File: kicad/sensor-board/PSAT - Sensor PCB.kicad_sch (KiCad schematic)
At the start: 19 parts, among them J1 MCU - Conn_01x01, J2 Conn_01x02, J3 MCU - Conn_01x02, J4 MCU - Conn_01x04, J5 Conn_01x01, U1 MPU-6000, U2 BME280

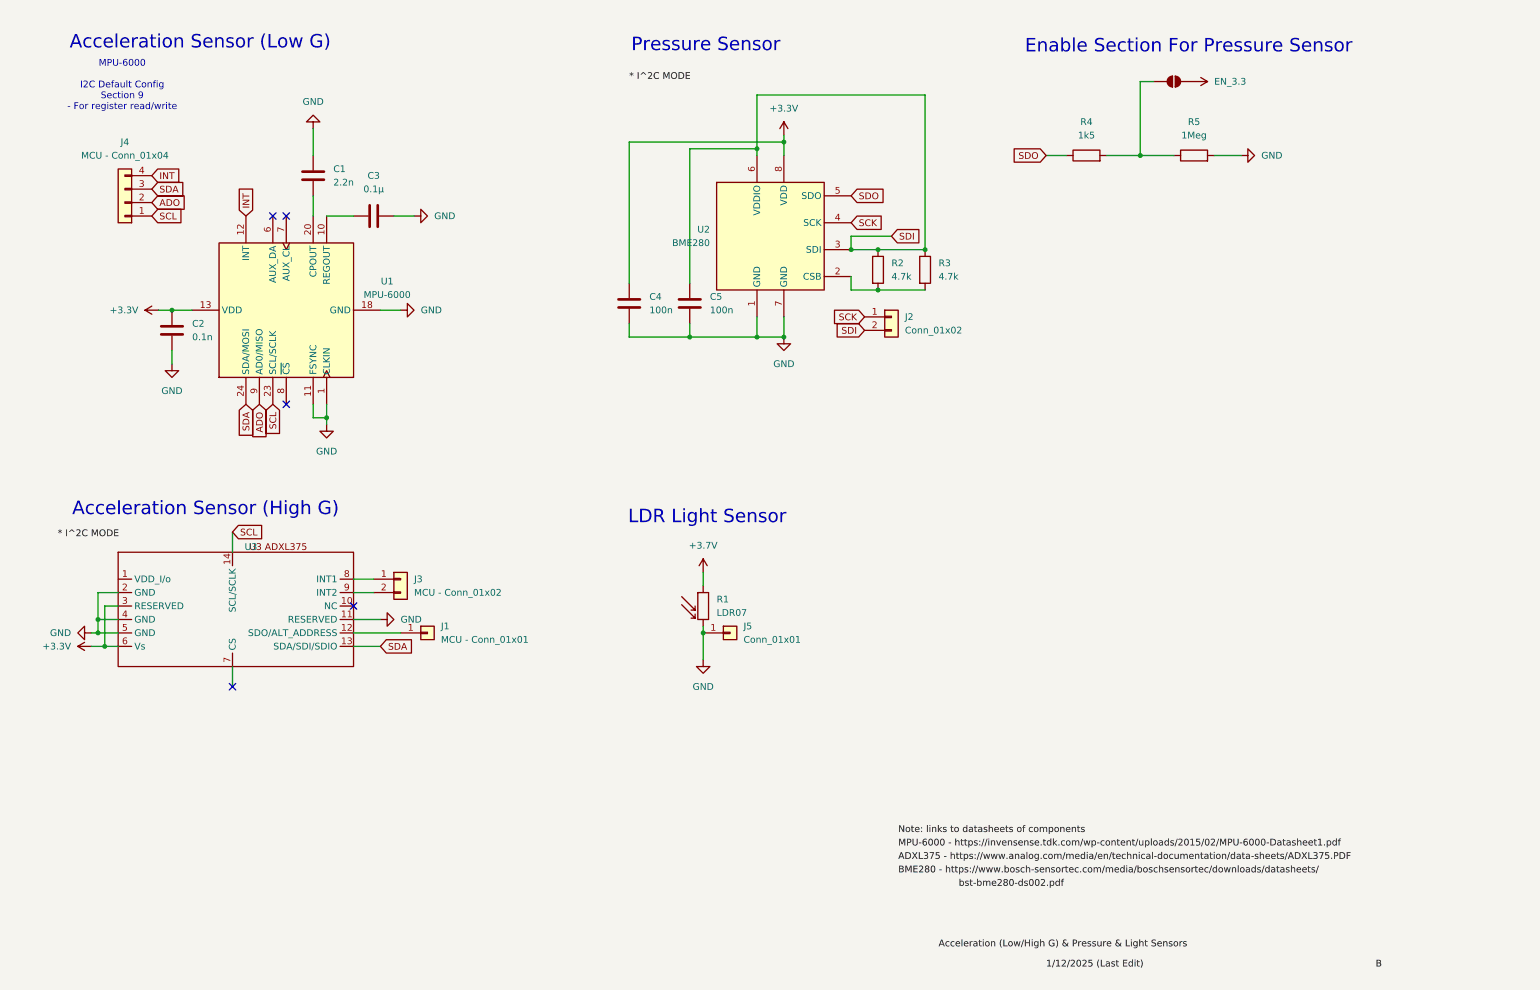
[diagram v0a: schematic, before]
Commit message: feat: sensor board schematic and started pcb
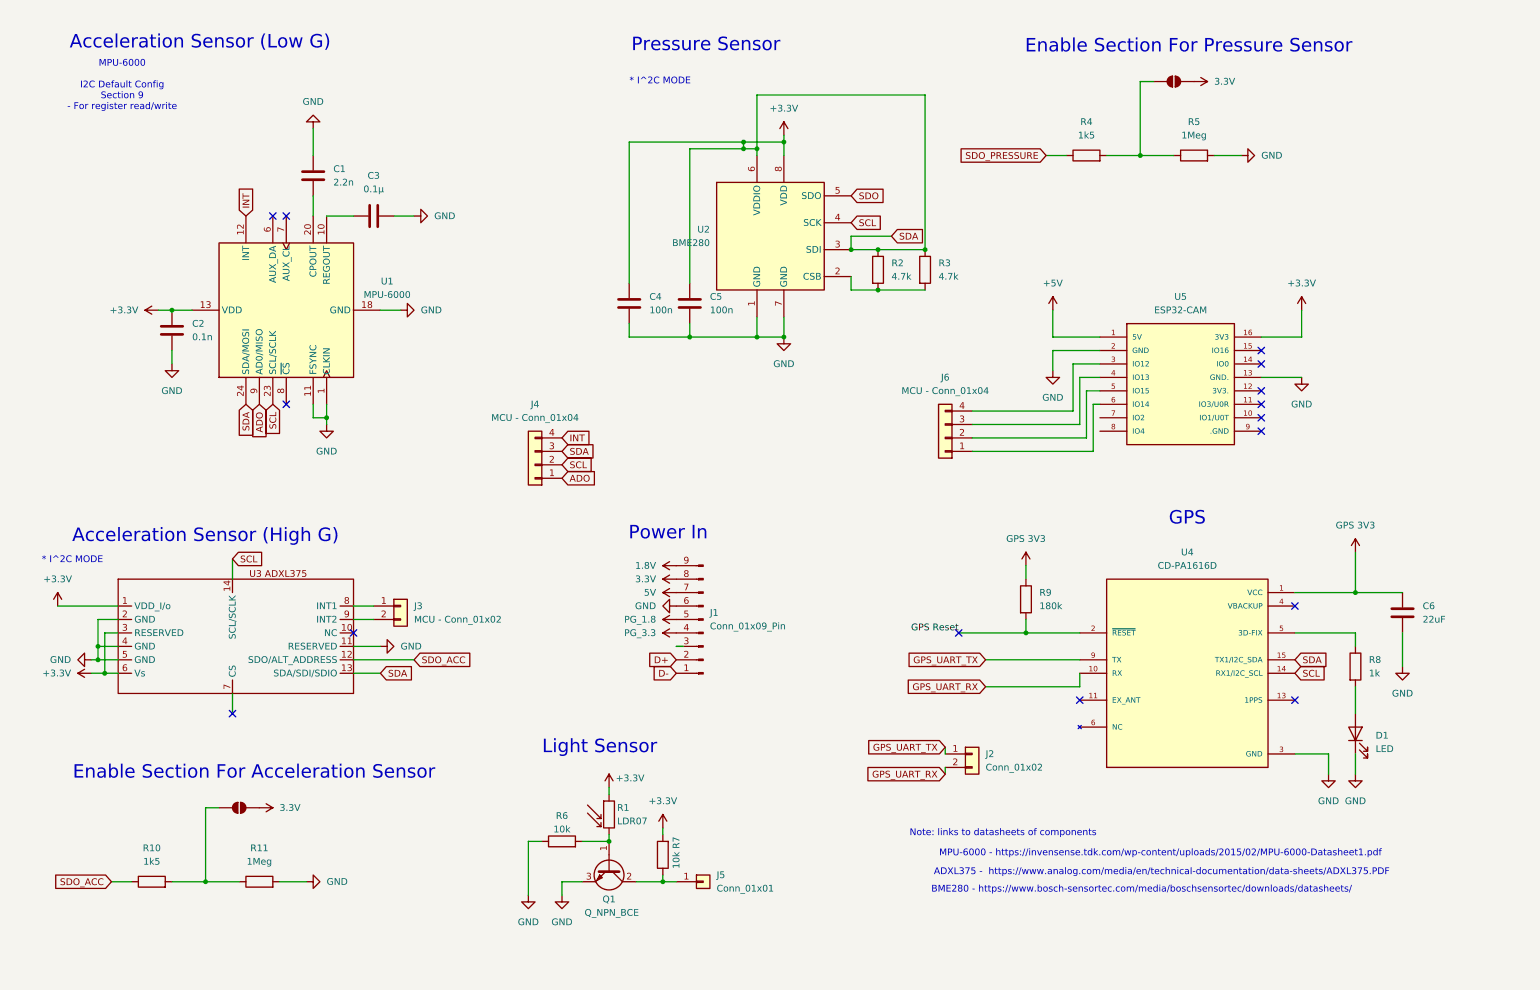
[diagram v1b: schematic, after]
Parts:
- removed J1: MCU - Conn_01x01, symbol Connector_Generic:Conn_01x01
- added C6: 22uF, Capacitor_SMD:C_0805_2012Metric_Pad1.18x1.45mm_HandSolder, symbol Device:C
- added D1: LED, LED_SMD:LED_LiteOn_LTST-C19HE1WT, symbol Device:LED
- added J1: Conn_01x09_Pin, Connector_PinHeader_2.54mm:PinHeader_1x09_P2.54mm_Vertical, symbol Connector:Conn_01x09_Pin
- added J6: MCU - Conn_01x04, Connector_PinHeader_2.54mm:PinHeader_1x04_P2.54mm_Vertical, symbol Connector_Generic:Conn_01x04
- added JP2: EN_5, Jumper:SolderJumper-2_P1.3mm_Open_Pad1.0x1.5mm, symbol Jumper:SolderJumper_2_Open
- added Q1: Q_NPN_BCE, Package_TO_SOT_SMD:SOT-23-3, symbol Transistor_BJT:Q_NPN_BCE
- added R10: 1k5, Resistor_SMD:R_0805_2012Metric_Pad1.20x1.40mm_HandSolder, symbol Device:R
- added R11: 1Meg, Resistor_SMD:R_0805_2012Metric_Pad1.20x1.40mm_HandSolder, symbol Device:R
- added R6, R7: 10k, Resistor_SMD:R_0805_2012Metric_Pad1.20x1.40mm_HandSolder, symbol Device:R
- added R8: 1k, Resistor_SMD:R_0805_2012Metric_Pad1.20x1.40mm_HandSolder, symbol Device:R
- added R9: 180k, Resistor_SMD:R_0805_2012Metric_Pad1.20x1.40mm_HandSolder, symbol Device:R
- added U4: CD-PA1616D, gps:XCVR_CD-PA1616D, symbol CD-PA1616D:CD-PA1616D
- added U5: ESP32-CAM, Connector_PinSocket_2.54mm:ESPCam, symbol ESP32-CAM:ESP32-CAM
- J2, J3: footprint (none) -> Connector_PinHeader_2.54mm:PinHeader_1x02_P2.54mm_Vertical
- J4: footprint (none) -> Connector_PinHeader_2.54mm:PinHeader_1x04_P2.54mm_Vertical
- J5: footprint (none) -> Connector_PinHeader_2.54mm:PinHeader_1x01_P2.54mm_Vertical
- R4, R5: footprint Resistor_SMD:R_0402_1005Metric -> Resistor_SMD:R_0805_2012Metric_Pad1.20x1.40mm_HandSolder
- U1: footprint (none) -> mpu6000:QFN-24-EP
- U2: footprint (none) -> bme280:PSON65P250X250X100-8N
- U3: value ~ -> ADXL375; footprint ADXL375:0805 CAP -> ADXL375:PQFN80P500X300X100-14N
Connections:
- net +3.7V is gone; now on net +3.3V: R1.1
- net SDA is gone; now on net +3.3V: J4.3 (Pin_3), U1.24 (SDA/MOSI), U3.13 (SDA/SDI/SDIO)
- net +3.3V: now also C5.1, R2.1, R3.1, U2.3 (SDI), U2.6 (VDDIO), U3.1 (VDD_I/o), R7.2, U4.15 (TX1/I2C_SDA), U5.16 (3V3)
- net ADO: now also J4.1 (Pin_1); no longer J4.2 (Pin_2)
- net GND: now also C6.2, D1.1 (K), J1.6 (Pin_6), Q1.3 (E), R11.2, R6.1, U4.12 (GND), U4.19 (GND), U4.3 (GND), U4.8 (GND), U5.13 (GND.), U5.2 (GND); no longer J5.1 (Pin_1), R1.2
- net SCL: now also J4.2 (Pin_2), U2.4 (SCK), U4.14 (RX1/I2C_SCL); no longer J4.1 (Pin_1)
- net SDO: no longer R4.1
- net SDO_ACC: now reaches U3.12 (SDO/ALT_ADDRESS)
- net SDO_ACC: now also R10.1
- net EN_3.3 renamed 3.3V
- net 3.3V: now also J1.8 (Pin_8), JP2.1 (A)
- net SCK renamed GPS_UART_TX
- net GPS_UART_TX: now also U4.9 (TX); no longer U2.4 (SCK)
- removed net SDI: C5.1, J2.2 (Pin_2), R2.1, R3.1, U2.3 (SDI), U2.6 (VDDIO)
- new net: D1.2 (A), R8.2
- new net: Q1.1 (B), R1.2, R6.2
- new net: J6.4 (Pin_4), U5.3 (IO12)
- new net: J6.3 (Pin_3), U5.4 (IO13)
- new net: J6.2 (Pin_2), U5.5 (IO15)
- new net: J6.1 (Pin_1), U5.6 (IO14)
- new net: U4.16 (NC), U4.17 (NC), U4.18 (NC), U4.20 (NC), U4.6 (NC), U4.7 (NC)
- new net: R8.1, U4.5 (3D-FIX)
- new net: J5.1 (Pin_1), Q1.2 (C), R7.1
- new net: JP2.2 (B), R10.2, R11.1
- new net +5V: U5.1 (5V)
- new net 1.8V: J1.9 (Pin_9)
- new net 5V: J1.7 (Pin_7)
- new net D+: J1.2 (Pin_2)
- new net D-: J1.1 (Pin_1)
- new net GPS 3V3: C6.1, R9.1, U4.1 (VCC)
- new net GPS Reset: R9.2, U4.2 (~{RESET})
- new net GPS_UART_RX: J2.2 (Pin_2), U4.10 (RX)
- new net PG_1.8: J1.5 (Pin_5)
- new net PG_3.3: J1.4 (Pin_4)
- new net SDO_PRESSURE: R4.1
- no-connect marks 5 -> 15
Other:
- note added: "* I^2C MODE"
- note added: "ADXL375 - https://www.analog.com/media/en/technical-documentation/data-sheets/ADXL375.PDF"
- note added: "BME280 - https://www.bosch-sensortec.com/media/boschsensortec/downloads/datasheets/"
- note added: "Enable Section For Acceleration Sensor"
- note added: "GPS"
- note added: "Light Sensor"
- note added: "MPU-6000 - https://invensense.tdk.com/wp-content/uploads/2015/02/MPU-6000-Datasheet1.pdf"
- note added: "Note: links to datasheets of components"
- note added: "Power In"
- note removed: "LDR Light Sensor"
- title: (none) -> Acceleration (Low/High G), Pressure, Light and GPS Sensors
- moved on the sheet: J2, J3, J4, J5, R1

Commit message: feat: sensor board pcb
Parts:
- removed J1: Conn_01x09_Pin, Connector_PinHeader_2.54mm:PinHeader_1x09_P2.54mm_Vertical, symbol Connector:Conn_01x09_Pin
- removed J3: MCU - Conn_01x02, Connector_PinHeader_2.54mm:PinHeader_1x02_P2.54mm_Vertical, symbol Connector_Generic:Conn_01x02
- removed J4: MCU - Conn_01x04, Connector_PinHeader_2.54mm:PinHeader_1x04_P2.54mm_Vertical, symbol Connector_Generic:Conn_01x04
- removed J5: Conn_01x01, Connector_PinHeader_2.54mm:PinHeader_1x01_P2.54mm_Vertical, symbol Connector_Generic:Conn_01x01
- added H1, H2, H3: MountingHole, MountingHole:MountingHole_3mm_Pad, symbol Mechanical:MountingHole
- added J1: Conn_01x06, Connector_PinHeader_2.54mm:PinHeader_1x06_P2.54mm_Vertical, symbol Connector_Generic:Conn_01x06
- added J3: Conn_01x03_Pin, Connector_PinHeader_2.54mm:PinHeader_1x03_P2.54mm_Vertical, symbol Connector:Conn_01x03_Pin
- added J4: Conn_01x03, Connector_PinHeader_2.54mm:PinHeader_1x03_P2.54mm_Vertical, symbol Connector_Generic:Conn_01x03
- added JP3, JP4: EN_5, Jumper:SolderJumper-2_P1.3mm_Open_Pad1.0x1.5mm, symbol Jumper:SolderJumper_2_Open
- D1: footprint LED_SMD:LED_LiteOn_LTST-C19HE1WT -> LED_SMD:LED_0805_2012Metric
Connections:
- net GPS 3V3 is gone; now on net 3.3V: C6.1, R9.1, U4.1 (VCC)
- net SDO is gone; now on net SDO_PRESSURE: U2.5 (SDO)
- net 3.3V: now also C2.1, C4.1, C5.1, R1.1, R3.1, R7.2, U1.13 (VDD), U2.6 (VDDIO), U2.8 (VDD), U3.1 (VDD_I/o), U3.3 (RESERVED), U3.6 (Vs), J3.1 (Pin_1), JP3.1 (A)
- net 5V: now also J3.2 (Pin_2), JP4.1 (A)
- net ADO: now also J1.1 (Pin_1)
- net GND: now also J3.3 (Pin_3)
- net INT: now also J4.1 (Pin_1)
- net at U3.8 (INT1): now also J4.2 (Pin_2)
- net at U3.9 (INT2): now also J4.3 (Pin_3)
- net LIGHT: now reaches Q1.2 (C), R7.1
- net LIGHT: now also J1.2 (Pin_2)
- removed net +3.3V: C2.1, C4.1, C5.1, R1.1, R2.1, R3.1, R7.2, U1.13 (VDD), U1.24 (SDA/MOSI), U2.3 (SDI), U2.6 (VDDIO), U2.8 (VDD), U3.1 (VDD_I/o), U3.13 (SDA/SDI/SDIO), U3.3 (RESERVED), U3.6 (Vs), U4.15 (TX1/I2C_SDA), U5.16 (3V3)
- net +5V: no longer names the net of U5.1 (5V)
- net +5V: now also JP4.2 (B)
- net SCL renamed SCL1
- net SCL1: now also J1.4 (Pin_4); no longer U1.23 (SCL/SCLK), U4.14 (RX1/I2C_SCL)
- new net: JP3.2 (B), U5.16 (3V3)
- new net SCL2: J1.3 (Pin_3), U1.23 (SCL/SCLK), U4.14 (RX1/I2C_SCL)
- new net SDA1: J1.6 (Pin_6), R2.1, U2.3 (SDI), U3.13 (SDA/SDI/SDIO)
- new net SDA2: J1.5 (Pin_5), U1.24 (SDA/MOSI), U4.15 (TX1/I2C_SDA)
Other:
- moved on the sheet: R3
